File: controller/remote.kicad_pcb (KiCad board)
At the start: 2 copper layers, 65.5 x 69.6 mm, 62 parts, among them J1 Conn_01x03, J10 Conn_01x03, J11 Conn_01x03, J12 Conn_01x02, J13 Conn_01x04, J14 Conn_01x04, J2 Conn_01x02, J3 Conn_01x07, J4 Conn_01x03, J5 Conn_01x03, J6 Conn_01x02, J7 Conn_01x03, J8 Conn_01x08, J9 Conn_01x08, SW1 SW_SPDT_MSM, SW10 SW_Push, SW11 SW_DP3T, SW2 SW_SPDT_MSM, SW3 SW_SPDT_MSM, SW4 SW_SPDT_MSM, SW5 SW_Push, SW6 SW_Push, SW7 SW_Push, SW8 SW_Push, SW9 SW_Push, U1 74LS165, U2 74LS165, U3 Arduino_Nano_v3.x, U4 AP1117, U5 nRF24L01+, U6 OLED_7pin_4SPI, U7 COM-09032, U8 COM-09032

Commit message: Update to 4-pin I2C display.
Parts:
- removed J1, J10, J11, J4, J5, J7: Conn_01x03, Milling:JST_XH_B03B-XH-A_1x03_P2.50mm_Vertical_Milling
- removed J12, J6: Conn_01x02, Milling:JST_XH_B02B-XH-A_1x02_P2.50mm_Vertical_Milling
- removed J13, J14: Conn_01x04, Milling:JST_XH_B04B-XH-A_1x04_P2.50mm_Vertical_Milling
- removed J3: Conn_01x07, Connector_JST:JST_XH_B07B-XH-A_1x07_P2.50mm_Vertical
- removed R1, R13, R14, R15, R16, R2, R3, R4, R5, R6, R7, R8: 10k, Resistor_SMD:R_0805_2012Metric
- removed R10, R11, R12, R9: 10K, Resistor_SMD:R_0805_2012Metric
- removed RV1, RV2: POT, Remote:Potentiometer_4mm_axis
- removed SW1, SW2, SW3, SW4: SW_SPDT_MSM, Remote:Switch_1x03_P5.08mm
- removed SW10, SW5, SW6, SW7, SW8, SW9: SW_Push, Remote:Switch_1x02_P6mm
- removed SW11: SW_DP3T, Remote:Switch_2x03_P3mm_Slide
- removed U7, U8: COM-09032, Remote:XDCR_COM-09032
- J2: value Conn_01x02 -> Conn_01x06; footprint Milling:JST_XH_B02B-XH-A_1x02_P2.50mm_Vertical_Milling -> Connector_JST:JST_XH_B06B-XH-A_1x06_P2.50mm_Vertical
- U1, U2: footprint Milling:DIP-16_W7.62mm_Milling -> Package_DIP:DIP-16_W7.62mm
- U6: value OLED_7pin_4SPI -> OLED_4pin_I2C; footprint Remote:Display_OLED_7pin_4SPI -> Remote:Display_OLED_4pin_I2C
- moved J2 158.6 mm to (284.0, 112.5), turned to 180 degrees
- moved H3 124.9 mm to (326.6, 142.0)
- moved H4 100.7 mm to (270.5, 142.0)
- moved C6 99.1 mm to (299.2, 141.2), turned to 270 degrees
- moved C7 88.3 mm to (296.9, 141.2), turned to 270 degrees
- moved H2 78.2 mm to (310.1, 98.8)
- moved H1 66.7 mm to (270.5, 98.8)
- moved C4 23.6 mm to (317.2, 111.4), turned to 90 degrees
- moved C3 23.2 mm to (317.2, 115.8), turned to 90 degrees
- moved C2 11.1 mm to (277.9, 120.7), turned to 180 degrees
- moved C1 10.6 mm to (294.6, 98.6)
- moved U4 9.66 mm to (323.6, 112.5)
- moved J9 7.96 mm to (319.5, 150.9)
- moved C5 7.58 mm to (316.7, 131.3)
- moved U5 6.86 mm to (318.3, 134.1)
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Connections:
- U3 pad 16: SCK -> SCK_RF
- U3 pad 19: Net-(J3-Pad1) -> Net-(J2-Pad1)
- U3 pad 20: Net-(J3-Pad2) -> Net-(J2-Pad2)
- U3 pad 21: Net-(J3-Pad3) -> Net-(J2-Pad3)
- U3 pad 22: Net-(J3-Pad4) -> Net-(J2-Pad4)
- U3 pad 23: Net-(J3-Pad5) -> SDA
- U3 pad 24: Net-(J3-Pad6) -> SCK
- U3 pad 25: Net-(J3-Pad7) -> Net-(J2-Pad5)
- U3 pad 26: PL -> Net-(J2-Pad6)
- U3 pad 5: CS -> PL
- U3 pad 6: DC -> Net-(U3-Pad6)
- U3 pad 7: RESET -> Net-(U3-Pad7)
- U3 pad 8: SDA -> Net-(U3-Pad8)
- U3 pad 9: SCK -> Net-(U3-Pad9)
- U5 pad 5: SCK -> SCK_RF
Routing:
- net GND: track 401.4 -> 0.00 mm
- net +5V: track 81.4 -> 0.00 mm
- net Net-(J13-Pad3): track 4.86 -> 0.00 mm
- net Net-(J13-Pad1): track 4.76 -> 0.00 mm
- net Net-(J14-Pad4): track 4.65 -> 0.00 mm
- net Net-(J14-Pad3): track 4.65 -> 0.00 mm
- net Net-(J13-Pad2): track 4.65 -> 0.00 mm
- net Net-(J14-Pad2): track 4.65 -> 0.00 mm
- net Net-(J14-Pad1): track 4.65 -> 0.00 mm
- net Net-(J13-Pad4): track 4.65 -> 0.00 mm
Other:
- board size 65.5 x 69.6 mm -> 65.5 x 61.5 mm

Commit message: Update schematic.
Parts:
- added J1: Conn_01x02, Connector_JST:JST_XH_B02B-XH-A_1x02_P2.50mm_Vertical, F.Cu at (326.9, 150.9)
- added J3: Conn_01x04, Connector_JST:JST_XH_B04B-XH-A_1x04_P2.50mm_Vertical, F.Cu at (264.2, 136.7)
- moved H2 15.9 mm to (326.0, 99.0)
- moved H4 6.61 mm to (266.0, 146.8)
- moved H1 4.51 mm to (266.0, 99.0)
- moved J9 1.27 mm to (318.3, 150.9)
- moved H3 1.20 mm to (326.0, 141.0)
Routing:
- net +5V: track 0.00 -> 205.7 mm, vias 0 -> 5
- net GND: track 0.00 -> 169.4 mm, vias 0 -> 1
- net CP: track 0.00 -> 62.8 mm
- net PL: track 0.00 -> 43.2 mm
- net +3V3: track 0.00 -> 33.2 mm
- net Net-(J3-Pad4): track 0.00 -> 31.4 mm
- net CE: track 0.00 -> 30.6 mm
- net Net-(U1-Pad9): track 0.00 -> 29.1 mm
- net Net-(J3-Pad3): track 0.00 -> 28.9 mm
- net CSN: track 0.00 -> 26.8 mm
- net SDA: track 0.00 -> 26.8 mm
- net SCK: track 0.00 -> 26.8 mm
- net MOSI: track 0.00 -> 25.8 mm
- net Net-(J3-Pad2): track 0.00 -> 25.6 mm
- net SCK_RF: track 0.00 -> 24.8 mm
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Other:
- board size 65.5 x 61.5 mm -> 69 x 61.5 mm
- board text added: "https://github.com/bullestock/remote/tree/master/controller"

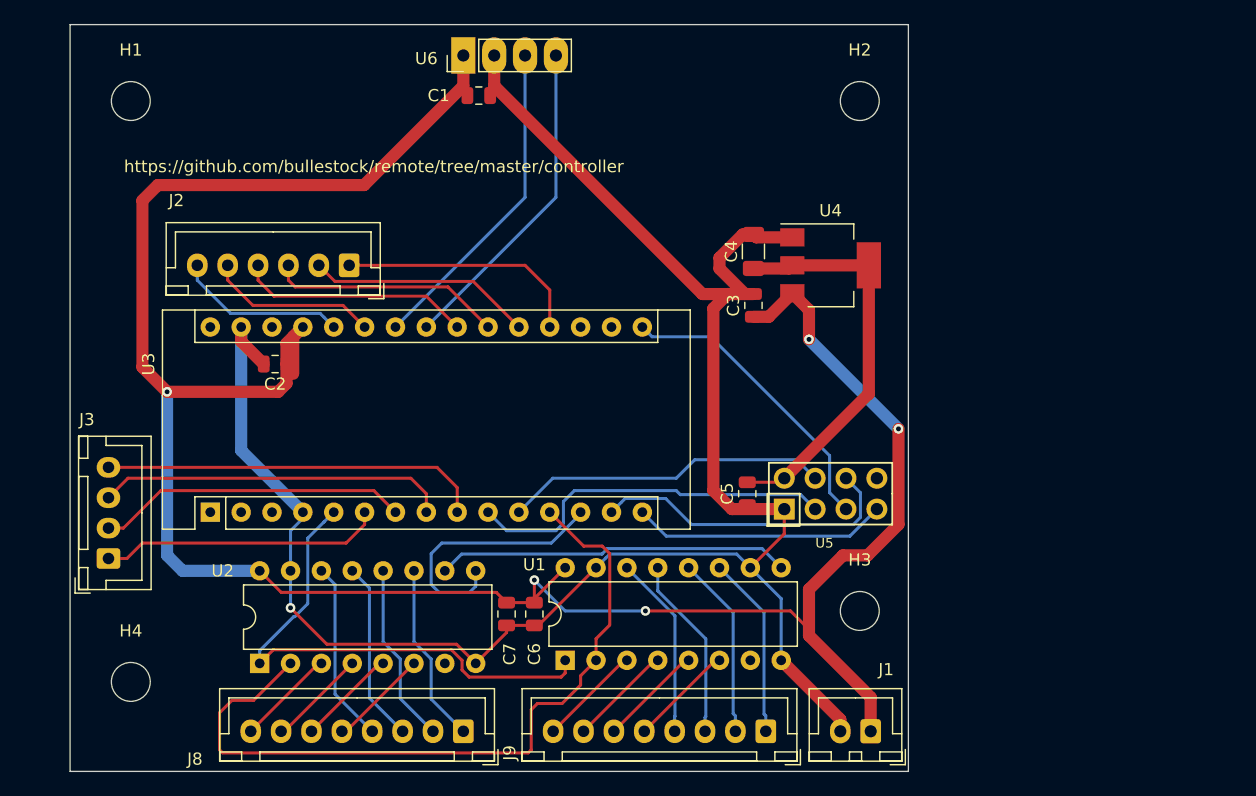
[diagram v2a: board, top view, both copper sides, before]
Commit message: Start migration to ESP32.
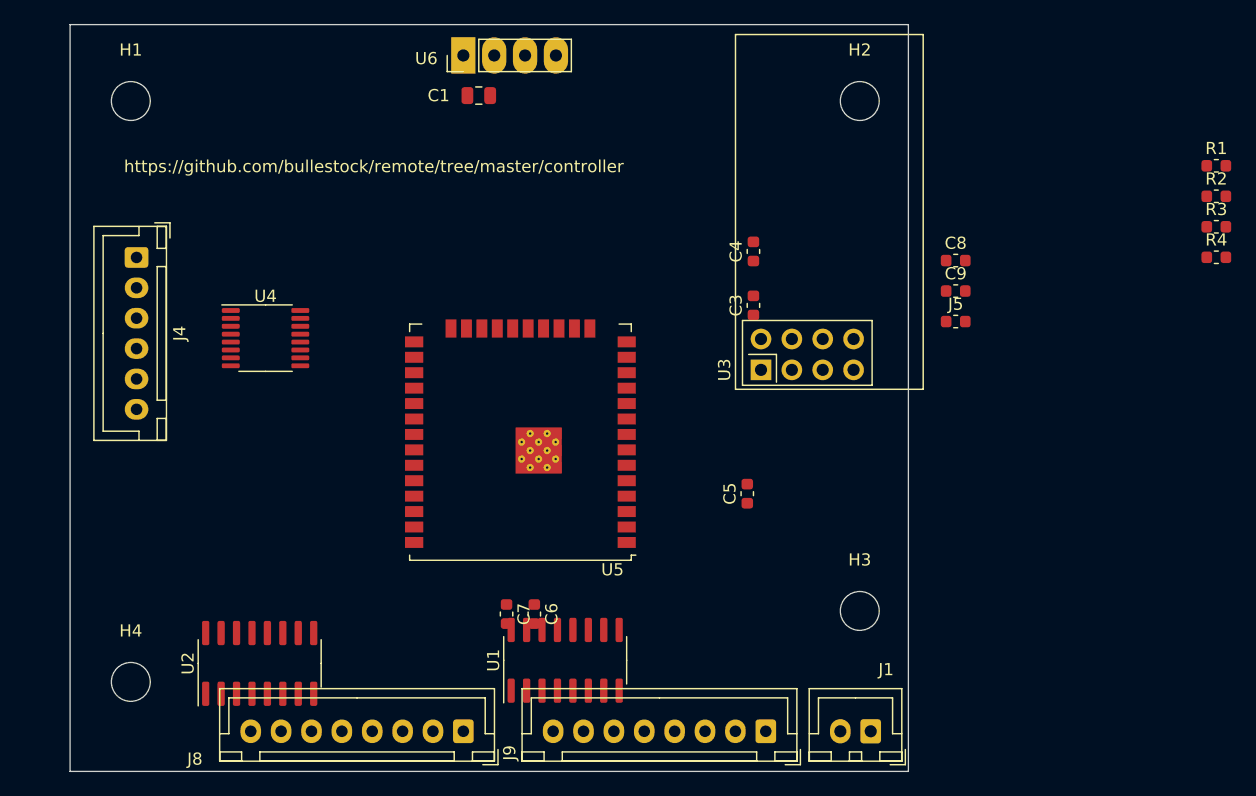
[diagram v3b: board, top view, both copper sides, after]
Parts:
- removed C2: 1u, Capacitor_SMD:C_0805_2012Metric
- removed J2: Conn_01x06, Connector_JST:JST_XH_B06B-XH-A_1x06_P2.50mm_Vertical
- removed J3: Conn_01x04, Connector_JST:JST_XH_B04B-XH-A_1x04_P2.50mm_Vertical
- added C8: 100n, Capacitor_SMD:C_0603_1608Metric, F.Cu at (333.9, 112.1)
- added C9: 10u, Capacitor_SMD:C_0603_1608Metric, F.Cu at (333.9, 114.6)
- added J4: Conn_01x06, Connector_JST:JST_XH_B06B-XH-A_1x06_P2.50mm_Vertical, F.Cu at (266.5, 111.9)
- added J5: Conn_01x02, Capacitor_SMD:C_0603_1608Metric, F.Cu at (333.9, 117.2)
- added R1: 0R, Capacitor_SMD:C_0603_1608Metric, F.Cu at (355.3, 104.3)
- added R2: 0R, Capacitor_SMD:C_0603_1608Metric, F.Cu at (355.3, 106.8)
- added R3: N/M, Resistor_SMD:R_0603_1608Metric, F.Cu at (355.3, 109.4)
- added R4: N/M, Resistor_SMD:R_0603_1608Metric, F.Cu at (355.3, 111.9)
- C3, C6, C7: footprint Capacitor_SMD:C_0805_2012Metric -> Capacitor_SMD:C_0603_1608Metric
- C4: value 22u -> 100n; footprint Capacitor_SMD:C_1206_3216Metric -> Capacitor_SMD:C_0603_1608Metric
- C5: value 1u -> C; footprint Capacitor_SMD:C_0805_2012Metric -> Capacitor_SMD:C_0603_1608Metric
- U1, U2: value 74LS165 -> 74HC165; footprint Package_DIP:DIP-16_W7.62mm -> Package_SO:SOP-16_3.9x9.9mm_P1.27mm
- U3: value Arduino_Nano_v3.x -> NRF24L01_Breakout; footprint Module:Arduino_Nano -> RF_Module:nRF24L01_Breakout
- U4: value AP1117 -> ADS7828; footprint Package_TO_SOT_SMD:SOT-223 -> Package_SO:TSSOP-16_4.4x5mm_P0.65mm
- U5: value nRF24L01+ -> ESP32-WROOM-32U; footprint Remote:nRF24L01 -> RF_Module:ESP32-WROOM-32U
- U6: value OLED_4pin_I2C -> MC130VX
- moved U4 46.9 mm to (277.1, 118.5)
- moved U3 46.8 mm to (317.9, 121.1)
- moved U5 21.4 mm to (298.1, 127.1)
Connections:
- C1 pad 1: +5V -> +3V3
- C3 pad 1: +5V -> +3V3
- C4 pad 1: +3V3 -> Net-(U4-REF)
- C4 pad 2: GND -> GNDS
- J1 pad 1: +5V -> +3V3
- U1 pad 7: Net-(U1-Pad7) -> unconnected-(U1-~{Q7}-Pad7)
- U2 pad 7: Net-(U2-Pad7) -> unconnected-(U2-~{Q7}-Pad7)
- U3 pad 1: Net-(U3-Pad1) -> GND
- U3 pad 2: Net-(U3-Pad2) -> +3V3
- U3 pad 3: Net-(U3-Pad3) -> CE
- U3 pad 4: GND -> CS
- U3 pad 5: PL -> SCK
- U3 pad 6: Net-(J3-Pad1) -> MOSI
- U3 pad 7: Net-(J3-Pad2) -> MISO
- U3 pad 8: Net-(J3-Pad3) -> unconnected-(U3-IRQ-Pad8)
- U4 pad 1: GND -> Net-(J4-Pin_1)
- U4 pad 2: +3V3 -> Net-(J4-Pin_2)
- U4 pad 3: +5V -> Net-(J4-Pin_3)
- U4 pad 4: +3V3 -> Net-(J4-Pin_4)
- U5 pad 3: CE -> unconnected-(U5-EN-Pad3)
- U5 pad 4: CSN -> unconnected-(U5-SENSOR_VP-Pad4)
- U5 pad 5: SCK_RF -> unconnected-(U5-SENSOR_VN-Pad5)
- U5 pad 6: MOSI -> unconnected-(U5-IO34-Pad6)
- U5 pad 7: MISO -> unconnected-(U5-IO35-Pad7)
- U5 pad 8: Net-(U5-Pad8) -> unconnected-(U5-IO32-Pad8)
- U6 pad GND: GND -> Net-(U6-2)
- U6 pad VDD: +5V -> Net-(U6-1)
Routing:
- net +5V: track 205.7 -> 0.00 mm, vias 5 -> 0
- net GND: track 169.4 -> 0.00 mm, vias 1 -> 0
- net CP: track 62.8 -> 0.00 mm
- net PL: track 43.2 -> 0.00 mm
- net +3V3: track 33.2 -> 0.00 mm
- net Net-(J3-Pad4): track 31.4 -> 0.00 mm
- net CE: track 30.6 -> 0.00 mm
- net Net-(U1-Q7): track 29.1 -> 0.00 mm
- net Net-(J3-Pad3): track 28.9 -> 0.00 mm
- net CSN: track 26.8 -> 0.00 mm
- net SDA: track 26.8 -> 0.00 mm
- net SCK: track 26.8 -> 0.00 mm
- net MOSI: track 25.8 -> 0.00 mm
- net Net-(J3-Pad2): track 25.6 -> 0.00 mm
- net SCK_RF: track 24.8 -> 0.00 mm
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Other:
- net class Default removed

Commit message: Work on routing.
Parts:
- removed J5: Conn_01x02, Capacitor_SMD:C_0603_1608Metric
- added C2: 10n, Capacitor_SMD:C_0603_1608Metric, F.Cu at (280.5, 113.0)
- added J2: Debug, Connector_PinHeader_2.54mm:PinHeader_1x06_P2.54mm_Vertical, F.Cu at (276.3, 94.4)
- added Q1: MMBT3904, Package_TO_SOT_SMD:SOT-23, F.Cu at (280.8, 109.4)
- added Q2: MMBT3904, Package_TO_SOT_SMD:SOT-23, F.Cu at (285.2, 109.4)
- added R5: 100k, Resistor_SMD:R_0603_1608Metric, F.Cu at (317.8, 132.4)
- added R6: 100k, Resistor_SMD:R_0603_1608Metric, F.Cu at (314.4, 132.4)
- J1: value Conn_01x02 -> Conn_01x03; footprint Connector_JST:JST_XH_B02B-XH-A_1x02_P2.50mm_Vertical -> Connector_JST:JST_XH_B03B-XH-A_1x03_P2.50mm_Vertical
- moved R4 64.4 mm to (292.0, 99.8), turned to -90 degrees
- moved R2 62.0 mm to (293.7, 100.8), turned to -90 degrees
- moved R1 59.9 mm to (295.5, 100.8), turned to -90 degrees
- moved R3 59.0 mm to (297.2, 99.8), turned to -90 degrees
- moved C4 40.0 mm to (280.0, 125.8), turned to -90 degrees
- moved C3 37.7 mm to (280.0, 122.0), turned to -90 degrees
- moved C7 25.8 mm to (272.3, 133.6), turned to 0 degrees
- moved C9 21.2 mm to (313.3, 119.7), turned to -90 degrees
- moved C8 20.2 mm to (315.1, 119.6), turned to -90 degrees
- moved J1 16.0 mm to (318.6, 137.2)
- moved U5 13.0 mm to (298.0, 114.1)
- moved C5 12.5 mm to (308.8, 121.7)
- moved C6 7.90 mm to (297.1, 133.6), turned to 0 degrees
- moved U2 6.95 mm to (276.4, 138.3)
- moved U1 6.72 mm to (301.2, 138.3)
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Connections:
- C1 pad 1: +3V3 -> Net-(U6-2)
- C1 pad 2: GND -> Net-(U6-1)
- C4 pad 2: GNDS -> GND
- C6 pad 1: +5V -> +3V3
- C7 pad 1: +5V -> +3V3
- J1 pad 1: +3V3 -> +BATT
- J1 pad 2: GND -> +3V3
- U1 pad 16: +5V -> +3V3
- U2 pad 16: +5V -> +3V3
- U4 pad 11: GNDS -> GND
- U4 pad 12: GNDS -> GND
- U4 pad 13: GNDS -> GND
- U4 pad 8: Net-(J5-Pin_2) -> GND
- U4 pad 9: GNDS -> GND
- U5 pad 13: unconnected-(U5-IO14-Pad13) -> Q7
- U5 pad 14: unconnected-(U5-IO12-Pad14) -> PL
- U5 pad 16: unconnected-(U5-IO13-Pad16) -> CP
- U5 pad 25: unconnected-(U5-IO0-Pad25) -> ~{BOOT}
- U5 pad 3: unconnected-(U5-EN-Pad3) -> ~{RESET}
- U5 pad 34: unconnected-(U5-RXD0/IO3-Pad34) -> MCU_RX0
- U5 pad 35: unconnected-(U5-TXD0/IO1-Pad35) -> MCU_TX0
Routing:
- net GND: track 0.00 -> 41.8 mm
- net +3V3: track 0.00 -> 23.3 mm
- net Net-(J8-Pin_1): track 0.00 -> 18.3 mm
- net Net-(J8-Pin_2): track 0.00 -> 17.7 mm
- net Net-(J9-Pin_1): track 0.00 -> 17.7 mm
- net Net-(J8-Pin_3): track 0.00 -> 17.5 mm
- net Net-(J9-Pin_2): track 0.00 -> 17.2 mm
- net Net-(J8-Pin_4): track 0.00 -> 17.1 mm
- net Net-(J9-Pin_3): track 0.00 -> 17.0 mm
- net Net-(J9-Pin_4): track 0.00 -> 16.8 mm
- net SDA: track 0.00 -> 16.6 mm
- net SCL: track 0.00 -> 12.6 mm
- net Net-(J4-Pin_1): track 0.00 -> 11.5 mm
- net Net-(J4-Pin_2): track 0.00 -> 10.0 mm
- net Net-(J4-Pin_3): track 0.00 -> 8.84 mm
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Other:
- board size 69 x 61.5 mm -> 69 x 58.7 mm

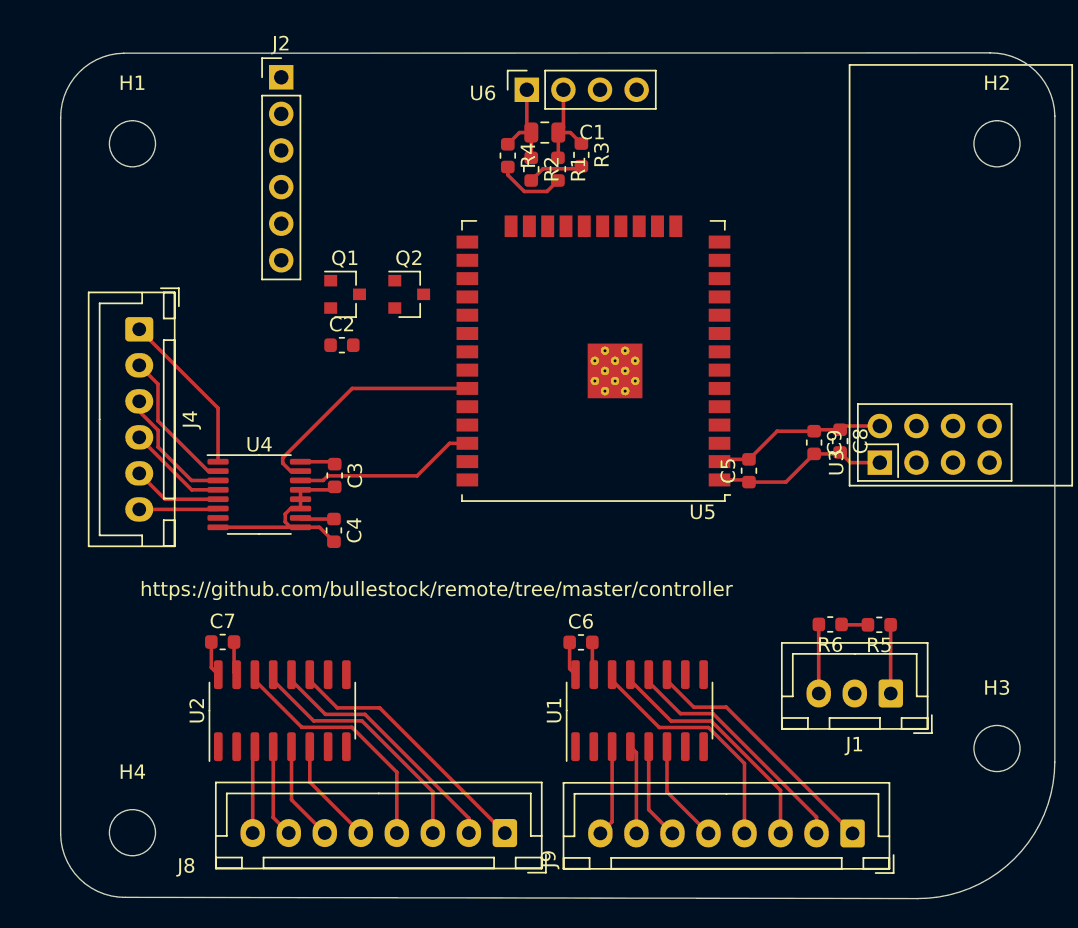
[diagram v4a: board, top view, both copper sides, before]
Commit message: Complete routing.
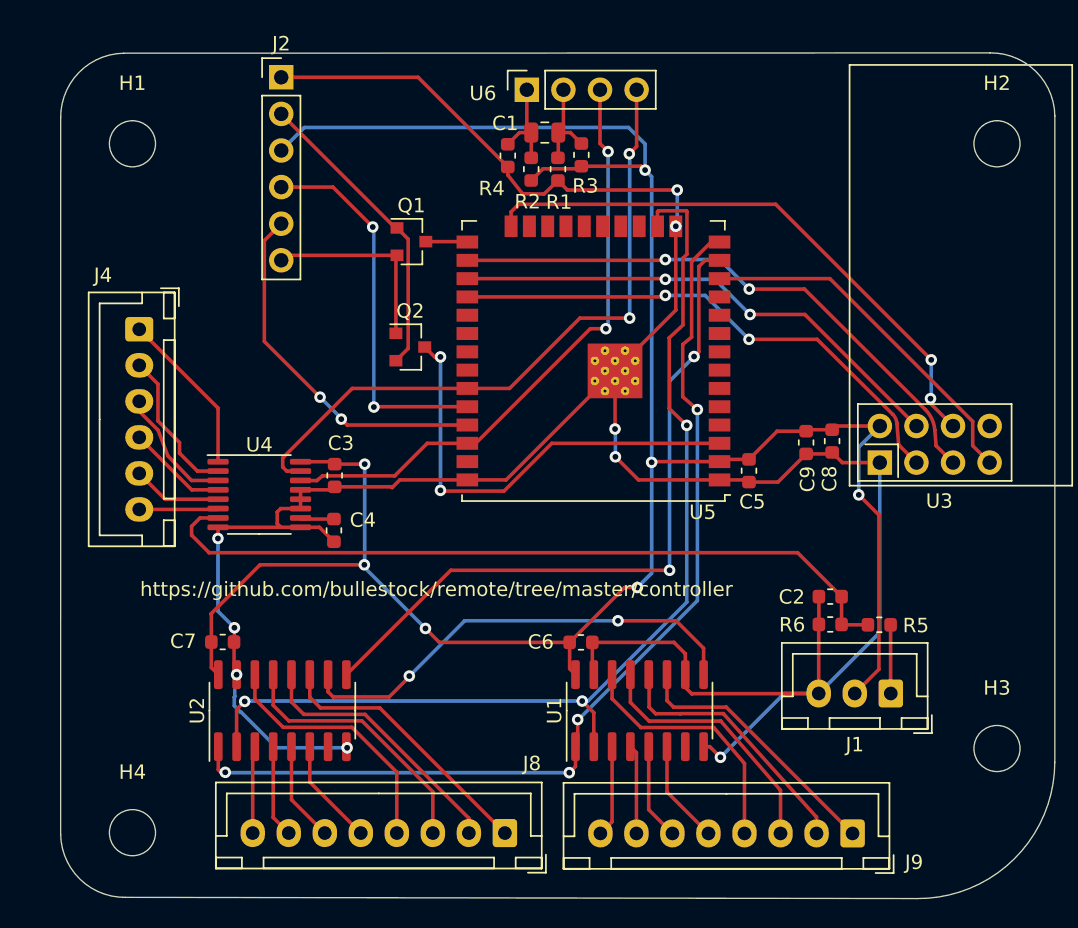
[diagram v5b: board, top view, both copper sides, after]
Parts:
- moved C2 38.1 mm to (314.4, 130.4), turned to 180 degrees
- moved Q1 5.88 mm to (285.4, 105.8)
- moved Q2 3.66 mm to (285.3, 113.1)
- moved C8 0.55 mm to (314.6, 119.6)
- moved C9 0.55 mm to (312.8, 119.7)
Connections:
- C1 pad 1: Net-(U6-2) -> Net-(U6-GND)
- C1 pad 2: Net-(U6-1) -> Net-(U6-VDD)
- R1 pad 1: Net-(U6-2) -> Net-(U6-GND)
- R2 pad 1: Net-(U6-1) -> Net-(U6-VDD)
- R3 pad 1: Net-(U6-2) -> Net-(U6-GND)
- R4 pad 1: Net-(U6-1) -> Net-(U6-VDD)
- U6 pad 1: (no net) -> Net-(U6-VDD)
- U6 pad 2: (no net) -> Net-(U6-GND)
- U6 pad 3: (no net) -> SCL
- U6 pad 4: (no net) -> SDA
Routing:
- net GND: track 41.8 -> 188.0 mm, vias 0 -> 9
- net +3V3: track 23.3 -> 156.8 mm, vias 0 -> 7
- net CP: track 0.00 -> 71.7 mm, vias 0 -> 3
- net PL: track 0.00 -> 68.5 mm, vias 0 -> 4
- net Net-(U4-CH6): track 1.84 -> 53.3 mm
- net Q7: track 0.00 -> 49.0 mm, vias 0 -> 2
- net SCK: track 0.00 -> 40.5 mm, vias 0 -> 2
- net MOSI: track 0.00 -> 40.1 mm, vias 0 -> 2
- net CE: track 0.00 -> 36.9 mm, vias 0 -> 2
- net CS: track 0.00 -> 35.4 mm, vias 0 -> 2
- net Net-(U1-Q7): track 0.00 -> 32.2 mm, vias 0 -> 2
- net ~{RESET}: track 0.00 -> 31.4 mm, vias 0 -> 2
- net SCL: track 12.6 -> 42.4 mm, vias 0 -> 2
- net SDA: track 16.6 -> 46.2 mm, vias 0 -> 2
- net MCU_RX0: track 0.00 -> 26.5 mm, vias 0 -> 2
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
